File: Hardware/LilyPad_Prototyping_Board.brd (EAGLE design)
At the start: 109.2 x 82.5 mm, 192 parts, among them J1 SEWTAP_LONG, J10 SEWTAP_LONG, J11 SEWTAP_LONG, J12 SEWTAP_LONG, J13 SEWTAP_LONG, J14 SEWTAP_LONG, J15 AMP FCI 10103594-0001LF, J2 SEWTAP_LONG, J3 SEWTAP_LONG, J4 SEWTAP_LONG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

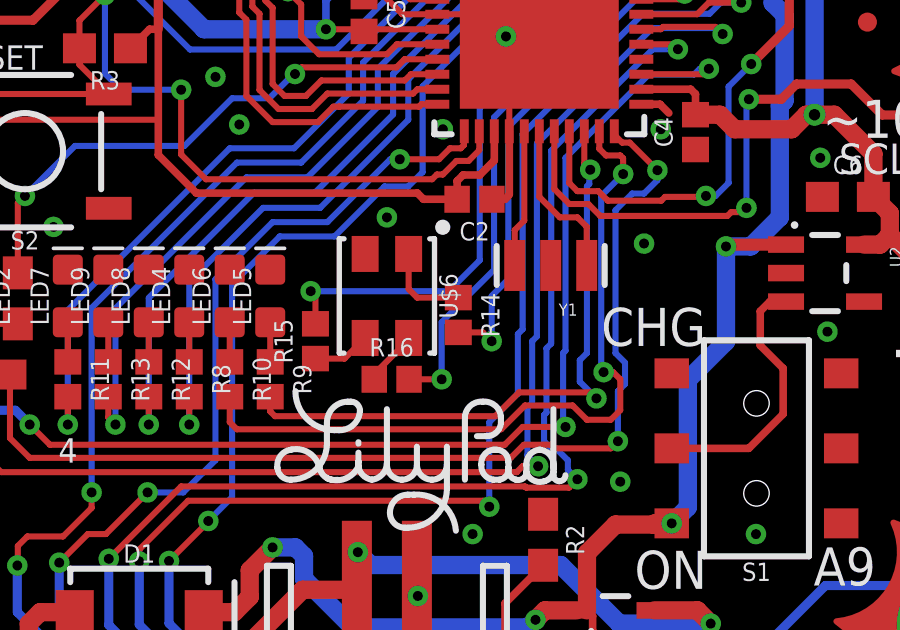
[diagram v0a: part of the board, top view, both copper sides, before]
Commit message: Tweaked a couple resistor values
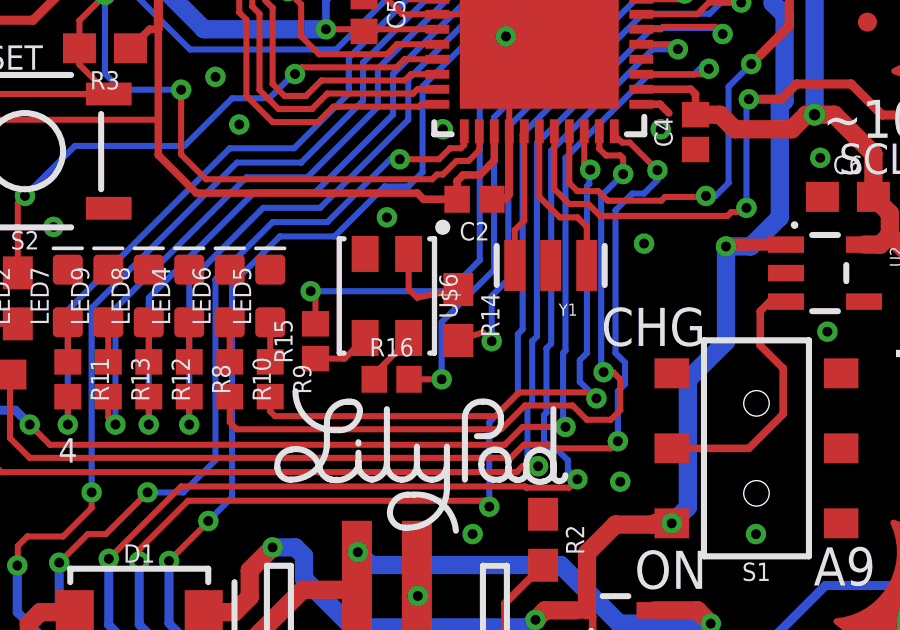
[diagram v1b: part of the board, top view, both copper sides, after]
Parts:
- R14: value 22 -> 330; device SparkFun-Resistors:0402 -> SparkFun-Resistors:0603
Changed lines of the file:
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@@
 <element name="U$33" library="newLilypadParts" package="PETAL_PAD_OFF" value="" x="-19.052540625" y="-11.000740625" rot="R30"/>
 <element name="U$34" library="newLilypadParts" package="PETAL_PAD_OFF" value="" x="8.94841875" y="20.09901875" rot="R246"/>
-<element name="R14" library="SparkFun-Resistors" package="0402" value="22" x="2.38125" y="-0.635" rot="R270">
-<attribute name="PROD_ID" value="RES-12427" x="2.38125" y="-0.635" size="1.778" layer="27" rot="R270" display="off"/>
+<element name="R14" library="SparkFun-Resistors" package="0603" value="330" x="2.38125" y="-0.635" rot="R270">
+<attribute name="PROD_ID" value="RES-00818" x="2.38125" y="-0.635" size="1.778" layer="27" rot="R270" display="off"/>
 </element>
 <element name="R15" library="SparkFun-Resistors" package="0402" value="22" x="-2.38125" y="-1.508125" rot="R90">
@@
 <element name="R25" library="SparkFun-Resistors" package="0603" value="100" x="-21.59" y="-40.3225" smashed="yes">
 <attribute name="NAME" x="-21.7805" y="-41.3385" size="0.8128" layer="25" font="vector" rot="R270"/>
-<attribute name="PROD_ID" value="RES-12438" x="-21.59" y="-40.3225" size="1.778" layer="27" display="off"/>
+<attribute name="PROD_ID" value="RES-07863" x="-21.59" y="-40.3225" size="1.778" layer="27" display="off"/>
 <attribute name="VALUE" value="100" x="-21.59" y="-40.3225" size="1.778" layer="27" display="off"/>
 </element>
 <element name="R26" library="SparkFun-Resistors" package="0603" value="100" x="-27.94" y="-40.3225" smashed="yes">
 <attribute name="NAME" x="-28.1305" y="-41.021" size="0.8128" layer="25" font="vector" rot="R270"/>
-<attribute name="PROD_ID" value="RES-12438" x="-27.94" y="-40.3225" size="1.778" layer="27" display="off"/>
+<attribute name="PROD_ID" value="RES-07863" x="-27.94" y="-40.3225" size="1.778" layer="27" display="off"/>
 <attribute name="VALUE" value="100" x="-27.94" y="-40.3225" size="1.778" layer="27" display="off"/>
 </element>
@@
 <element name="R29" library="SparkFun-Resistors" package="0603" value="100" x="11.43" y="-40.3225" smashed="yes">
 <attribute name="NAME" x="11.2395" y="-41.3385" size="0.8128" layer="25" font="vector" rot="R270"/>
-<attribute name="PROD_ID" value="RES-12438" x="11.43" y="-40.3225" size="1.778" layer="27" display="off"/>
+<attribute name="PROD_ID" value="RES-07863" x="11.43" y="-40.3225" size="1.778" layer="27" display="off"/>
 <attribute name="VALUE" value="100" x="11.43" y="-40.3225" size="1.778" layer="27" display="off"/>
 </element>
 <element name="R30" library="SparkFun-Resistors" package="0603" value="100" x="5.08" y="-40.3225" smashed="yes">
 <attribute name="NAME" x="4.8895" y="-41.021" size="0.8128" layer="25" font="vector" rot="R270"/>
-<attribute name="PROD_ID" value="RES-12438" x="5.08" y="-40.3225" size="1.778" layer="27" display="off"/>
+<attribute name="PROD_ID" value="RES-07863" x="5.08" y="-40.3225" size="1.778" layer="27" display="off"/>
 <attribute name="VALUE" value="100" x="5.08" y="-40.3225" size="1.778" layer="27" display="off"/>
 </element>
@@
 <wire x1="4.048125" y1="0.555625" x2="3.4925" y2="0" width="0.2032" layer="16"/>
 <via x="3.4925" y="-1.508125" extent="1-16" drill="0.3302"/>
-<wire x1="2.38125" y1="-1.215" x2="3.199375" y2="-1.215" width="0.2032" layer="1"/>
+<wire x1="2.38125" y1="-1.485" x2="3.199375" y2="-1.215" width="0.2032" layer="1"/>
 <wire x1="3.199375" y1="-1.215" x2="3.4925" y2="-1.508125" width="0.2032" layer="1"/>
 <wire x1="3.4925" y1="0" x2="3.4925" y2="-1.508125" width="0.2032" layer="16"/>
@@
 <wire x1="0.725" y1="1.4" x2="0.725" y2="0.2275" width="0.2032" layer="1"/>
 <wire x1="0.725" y1="0.2275" x2="1.0075" y2="-0.055" width="0.2032" layer="1"/>
-<wire x1="1.0075" y1="-0.055" x2="2.38125" y2="-0.055" width="0.2032" layer="1"/>
+<wire x1="1.0075" y1="-0.055" x2="2.38125" y2="0.215" width="0.2032" layer="1"/>
 </signal>
 <signal name="N$41">

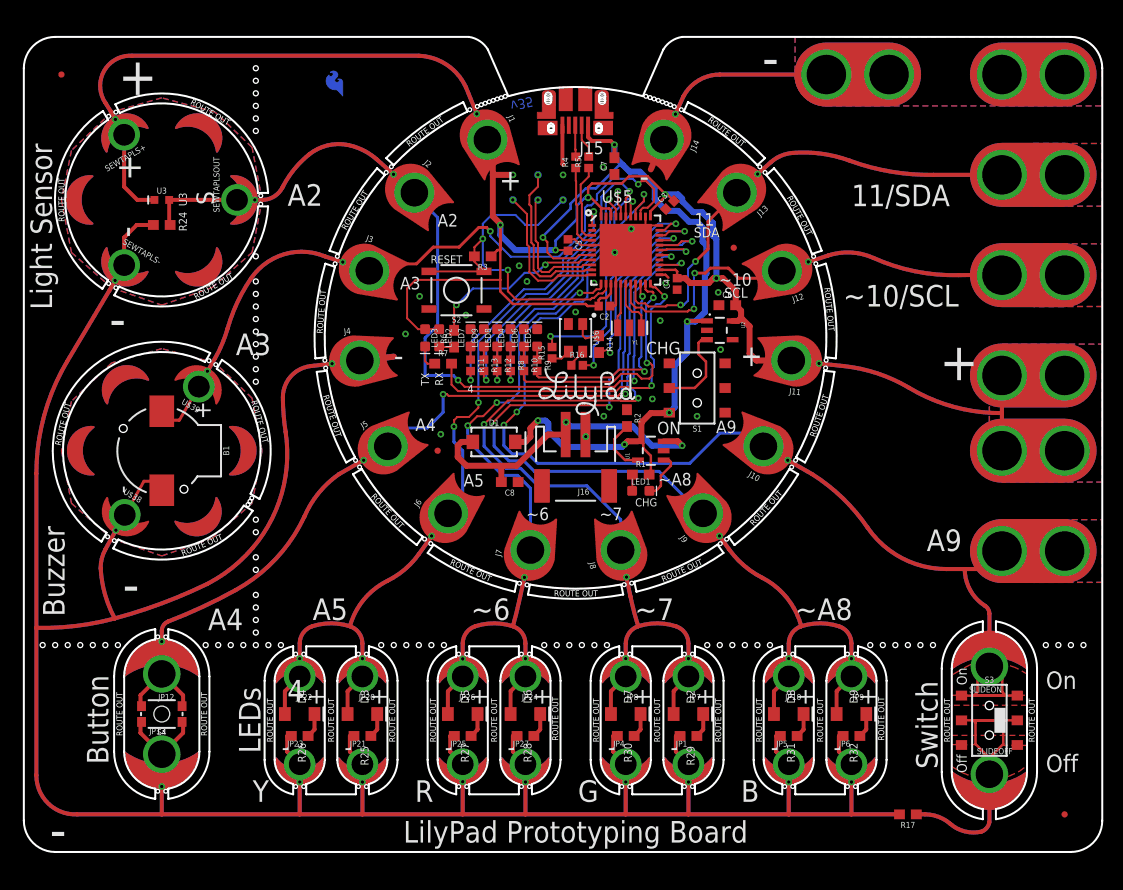
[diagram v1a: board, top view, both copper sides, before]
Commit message: Fixed some stop/lilypad tab errors
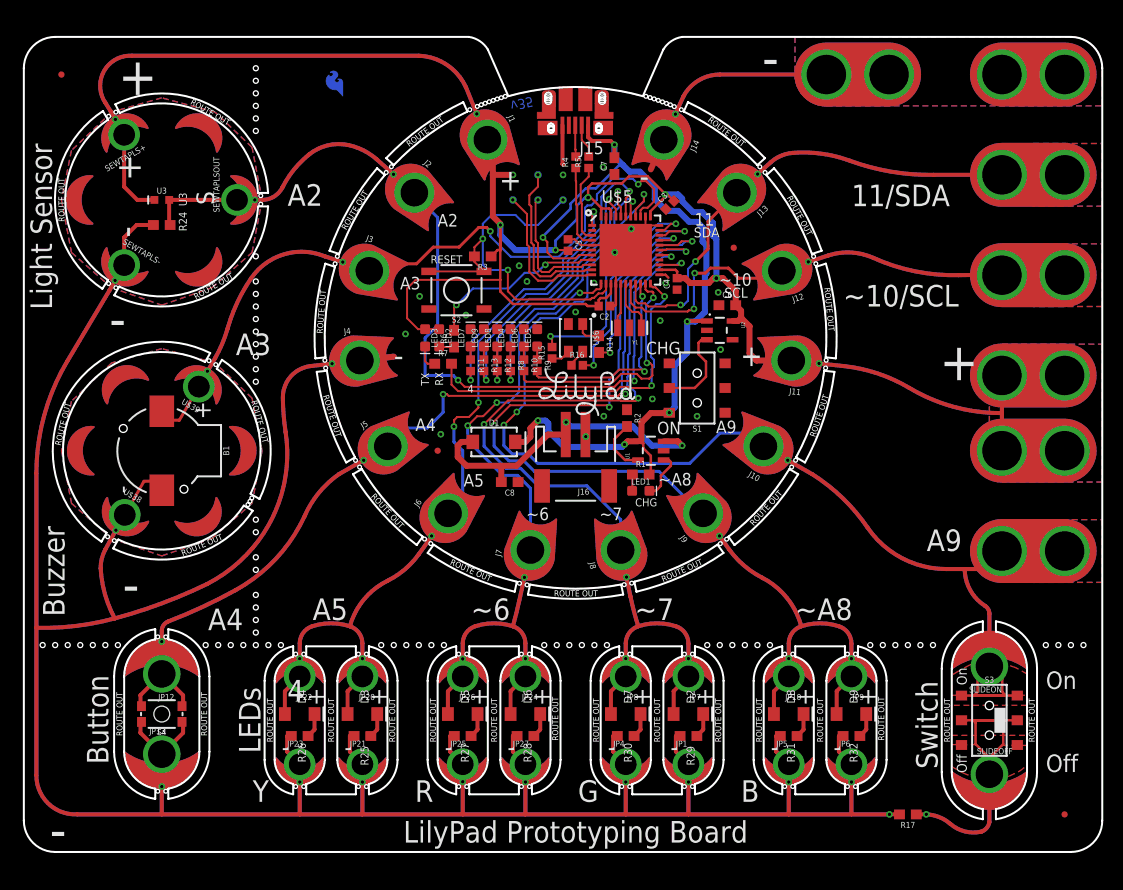
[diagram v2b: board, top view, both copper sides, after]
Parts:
- J1, J10, J11, J12, J13, J14, J2, J3, J4, J5, J6, J7, J8, J9: value SEWTAP_LONG -> SEWTAP_LONG-2SIDE; device LilyPad-Wearables:PETAL-LONG-1 -> LilyPad-Wearables:PETAL-LONG-1-2SIDE
- U$38, U$39: value SEWTAP_SMALL -> SEWTAP_SMALL-2SIDE; device LilyPad-Wearables:PETAL-SMALL -> LilyPad-Wearables:PETAL-SMALL-2SIDE
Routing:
- net GND: track 637.2 -> 636.0 mm, vias 33 -> 34
- net SW_CM1: track 13.0 -> 12.1 mm
- net SW_CM: track 32.4 -> 32.5 mm, vias 0 -> 1

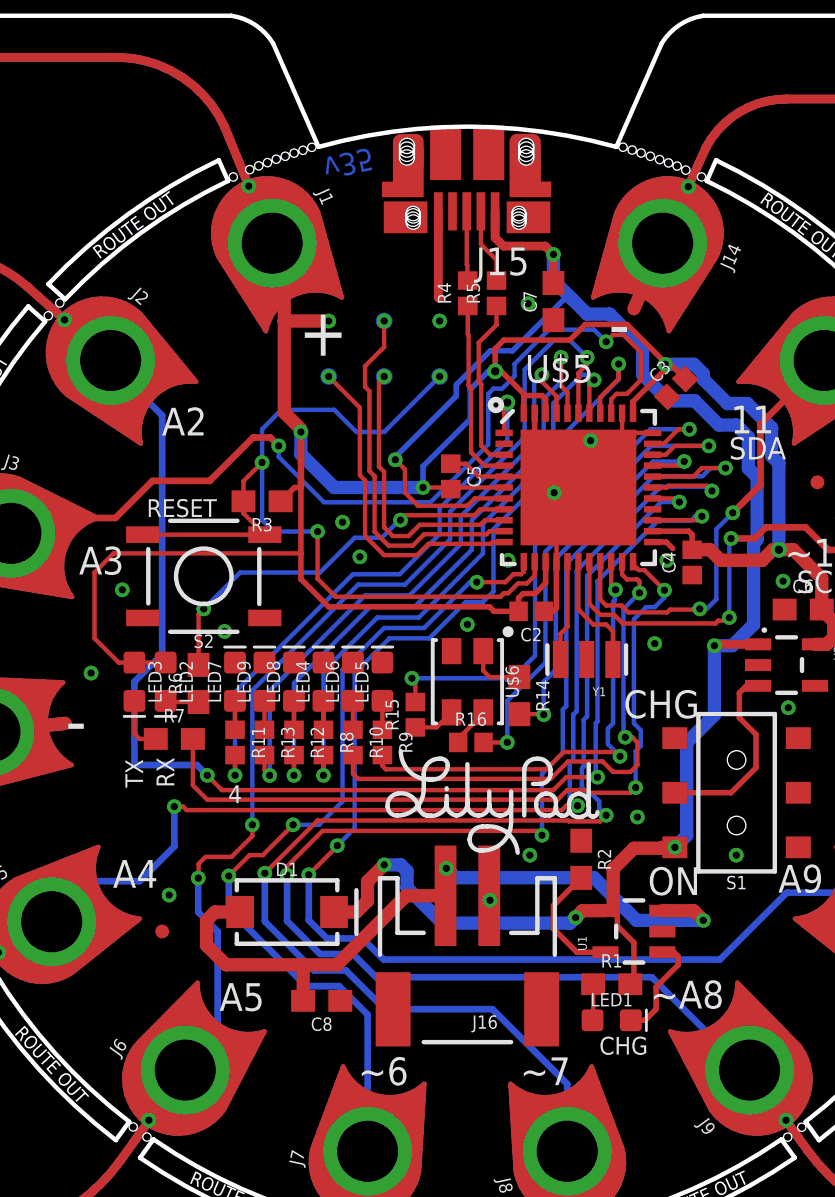
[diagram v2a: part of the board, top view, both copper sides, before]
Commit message: Addressed DFM errors
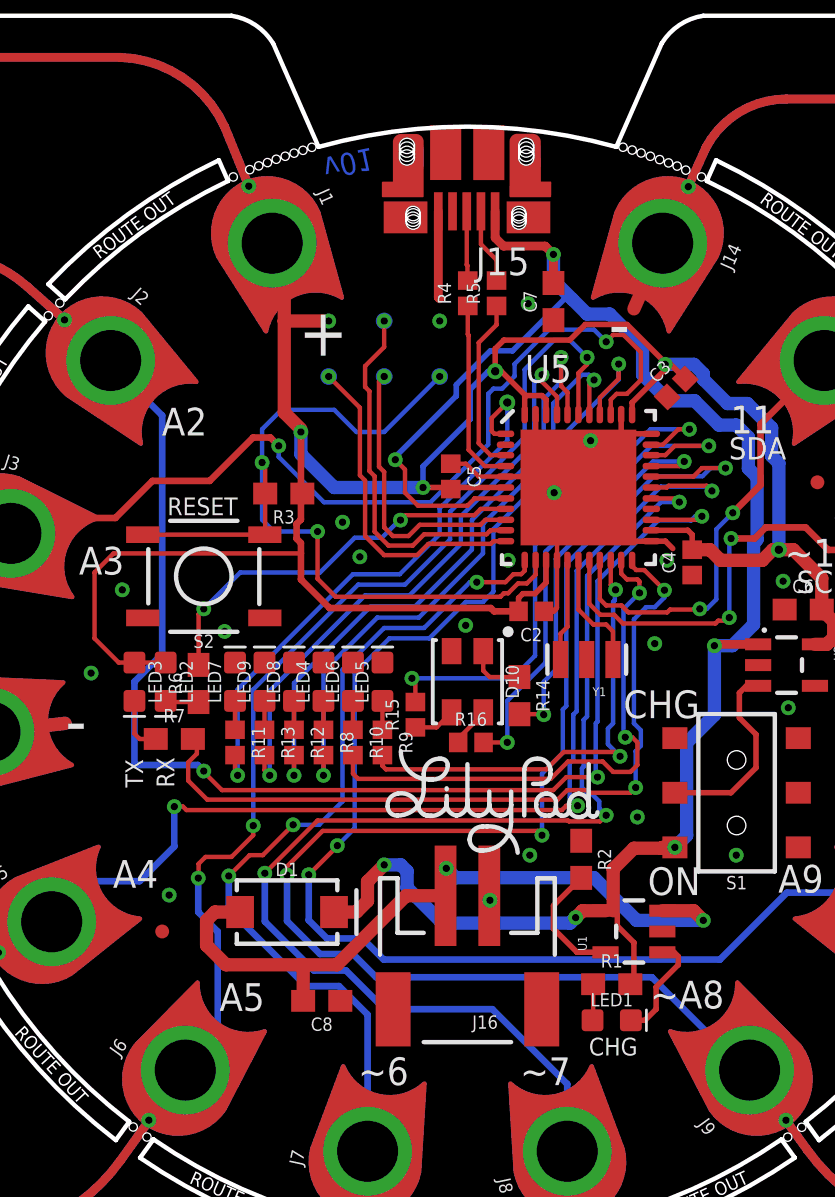
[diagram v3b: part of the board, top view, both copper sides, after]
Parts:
- removed U$5: 32U4, newLilypadParts:QFN-44
- added U5: ATMEGA32U4_NOARDQFN3, newLilypadParts:QFN-44-PAD_1:1-LESS_PASTE
- moved R3 1.05 mm to (-8.41, 8.61)
- renumbered U$6 to D10
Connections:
- net 3.3V: now also U5.14, U5.24, U5.34, U5.42, U5.44, U5.6; no longer U$5.14, U$5.24, U$5.34, U$5.42, U$5.44, U$5.6
- net BG_LED0: now also U5.38; no longer U$5.38
- net BG_LED1: now also U5.20; no longer U$5.20
- net BG_LED2: now also U5.21; no longer U$5.21
- net BG_LED3: now also U5.1; no longer U$5.1
- net BG_LED4: now also U5.40; no longer U$5.40
- net BG_LED5: now also U5.41; no longer U$5.41
- net D+: now also U5.4; no longer U$5.4
- net D-: now also U5.3; no longer U$5.3
- net D10: now also U5.18; no longer U$5.18
- net D11: now also U5.19; no longer U$5.19
- net D2: now also U5.25; no longer U$5.25
- net D25: now also U5.26; no longer U$5.26
- net D3: now also U5.36; no longer U$5.36
- net D4: now also U5.28; no longer U$5.28
- net D5: now also U5.39; no longer U$5.39
- net D6: now also U5.12; no longer U$5.12
- net D7: now also U5.27; no longer U$5.27
- net D8: now also U5.29; no longer U$5.29
- net D9: now also U5.37; no longer U$5.37
- net GND: now also U5.15, U5.23, U5.33, U5.35, U5.43, U5.5; no longer U$5.15, U$5.23, U$5.33, U$5.35, U$5.43, U$5.5
- net MISO: now also U5.11; no longer U$5.11
- net MOSI: now also U5.10; no longer U$5.10
- net N$5: now also U5.17; no longer U$5.17
- net N$7: now also U5.16; no longer U$5.16
- net RESET: now also U5.13; no longer U$5.13
- net RGB_B: now also U5.32; no longer U$5.32
- net RGB_G: now also U5.31; no longer U$5.31
- net RGB_R: now also U5.30; no longer U$5.30
- net RX_LED: now also U5.8; no longer U$5.8
- net SCK: now also U5.9; no longer U$5.9
- net TX_LED: now also U5.22; no longer U$5.22
- net VCC_1: now also U5.7; no longer U$5.7
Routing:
- net 3.3V: track 312.5 -> 307.0 mm
- net GND: track 636.0 -> 637.6 mm
- net BG_LED3: track 25.9 -> 26.7 mm
- net RESET: track 40.0 -> 39.4 mm
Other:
- board text added: "v01"
- board text removed: "v35"

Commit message: Added extra test points
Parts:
- added TP5, TP6, TP7, TP8: TEST-POINT3, SparkFun-Connectors:PAD.03X.03
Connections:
- net 3.3V: now also TP6.P$1
- net GND: now also TP5.P$1
- net N$2: now also TP8.P$1
- net V_BATT: now also TP7.P$1
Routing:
- net N$2: track 8.92 -> 9.94 mm, vias 0 -> 1
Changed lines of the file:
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@@
 <layer number="21" name="tPlace" color="16" fill="1" visible="yes" active="yes"/>
 <layer number="22" name="bPlace" color="14" fill="1" visible="yes" active="yes"/>
-<layer number="23" name="tOrigins" color="15" fill="1" visible="no" active="yes"/>
-<layer number="24" name="bOrigins" color="15" fill="1" visible="no" active="yes"/>
+<layer number="23" name="tOrigins" color="15" fill="1" visible="yes" active="yes"/>
+<layer number="24" name="bOrigins" color="15" fill="1" visible="yes" active="yes"/>
 <layer number="25" name="tNames" color="7" fill="1" visible="no" active="yes"/>
 <layer number="26" name="bNames" color="7" fill="1" visible="no" active="yes"/>
@@
 <attribute name="PROD_ID" value="DIO-13722" x="0" y="0" size="1.778" layer="27" rot="R270" display="off"/>
 </element>
+<element name="TP5" library="SparkFun-Connectors" package="PAD.03X.03" value="TEST-POINT3" x="-1.27" y="16.51" rot="MR0"/>
+<element name="TP6" library="SparkFun-Connectors" package="PAD.03X.03" value="TEST-POINT3" x="-6.35" y="16.51" rot="MR0"/>
+<element name="TP7" library="SparkFun-Connectors" package="PAD.03X.03" value="TEST-POINT3" x="10.795" y="-10.9140625" rot="MR0"/>
+<element name="TP8" library="SparkFun-Connectors" package="PAD.03X.03" value="TEST-POINT3" x="13.335" y="-5.08" rot="MR0"/>
 </elements>
 <signals>
@@
 <contactref element="U2" pad="3"/>
 <wire x1="9.49399375" y1="-5.08" x2="12.065" y2="-5.08" width="0.254" layer="1"/>
-<wire x1="12.065" y1="-5.08" x2="13.208" y2="-3.937" width="0.254" layer="1"/>
+<wire x1="12.065" y1="-5.08" x2="12.5015625" y2="-4.6434375" width="0.254" layer="1"/>
+<wire x1="12.5015625" y1="-4.6434375" x2="13.208" y2="-3.937" width="0.254" layer="1"/>
 <wire x1="13.208" y1="-3.937" x2="13.208" y2="-2.413" width="0.254" layer="1"/>
 <wire x1="13.208" y1="-2.413" x2="12.446" y2="-1.651" width="0.254" layer="1"/>
@@
 <wire x1="12.446" y1="-0.508" x2="12.766" y2="-0.188" width="0.254" layer="1"/>
 <wire x1="12.766" y1="-0.188" x2="13.3049" y2="-0.188" width="0.254" layer="1"/>
+<contactref element="TP8" pad="P$1"/>
+<wire x1="12.5015625" y1="-4.6434375" x2="12.938125" y2="-5.08" width="0.254" layer="1"/>
+<wire x1="12.938125" y1="-5.08" x2="13.335" y2="-5.08" width="0.254" layer="1"/>
+<via x="13.335" y="-5.08" extent="1-16" drill="0.3302"/>
 </signal>
 <signal name="V_BATT">
@@
 <wire x1="-11.938" y1="-10.922" x2="-11.557" y2="-10.541" width="0.6096" layer="1"/>
 <wire x1="-11.557" y1="-10.541" x2="-10.404996875" y2="-10.541" width="0.6096" layer="1"/>
-<wire x1="8.9201" y1="-10.48000625" x2="10.35300625" y2="-10.48000625" width="0.6096" layer="1"/>
-<wire x1="10.35300625" y1="-10.48000625" x2="10.795" y2="-10.922" width="0.6096" layer="1"/>
-<via x="10.795" y="-10.922" extent="1-16" drill="0.3302"/>
-<wire x1="10.795" y1="-10.922" x2="7.747" y2="-10.922" width="0.6096" layer="16"/>
+<wire x1="8.9201" y1="-10.48000625" x2="10.36094375" y2="-10.48000625" width="0.6096" layer="1"/>
+<via x="10.795" y="-10.9140625" extent="1-16" drill="0.3302"/>
 <via x="-0.968375" y="-8.54075" extent="1-16" drill="0.3302"/>
 <wire x1="-7.517503125" y1="-14.604996875" x2="-7.517503125" y2="-13.056496875" width="0.6096" layer="1"/>
@@
 <wire x1="-1" y1="-9.79375" x2="-1" y2="-8.572375" width="0.6096" layer="1"/>
 <wire x1="-1" y1="-8.572375" x2="-0.968375" y2="-8.54075" width="0.6096" layer="1"/>
+<contactref element="TP7" pad="P$1"/>
+<wire x1="7.747" y1="-10.922" x2="10.795" y2="-10.922" width="0.6096" layer="16"/>
+<wire x1="10.795" y1="-10.922" x2="10.795" y2="-10.9140625" width="0.6096" layer="16"/>
+<wire x1="10.36094375" y1="-10.48000625" x2="10.795" y2="-10.9140625" width="0.6096" layer="1"/>
 </signal>
 <signal name="GND">
@@
 <wire x1="4.101134375" y1="5.5535" x2="4.101134375" y2="7.606678125" width="0.2032" layer="1"/>
 <wire x1="4.101134375" y1="7.606678125" x2="4.0878125" y2="7.62" width="0.2032" layer="1"/>
+<contactref element="TP5" pad="P$1"/>
 </signal>
 <signal name="N$3">
@@
 <wire x1="-7.55580625" y1="8.612190625" x2="-7.55580625" y2="8.82580625" width="0.2032" layer="1"/>
 <wire x1="-7.55580625" y1="8.82580625" x2="-7.62" y2="8.89" width="0.2032" layer="1"/>
+<contactref element="TP6" pad="P$1"/>
 <wire x1="-7.62" y1="11.43" x2="-7.62" y2="11.557" width="0" layer="19" extent="1-16"/>
 </signal>
